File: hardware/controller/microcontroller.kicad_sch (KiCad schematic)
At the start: 41 parts, among them J1 USB_C_Receptacle_USB2.0_14P, J2 IDC-10, SW1 SW_Push, SW2 SW_Push, SW3 SW_Push, U1 SRV05-4, U2 ESP32-C3-WROOM-02, U3 STM32U535RET6, U4 nRF24L01+ 2.4Gz Mini SMD, Y1 8MHz

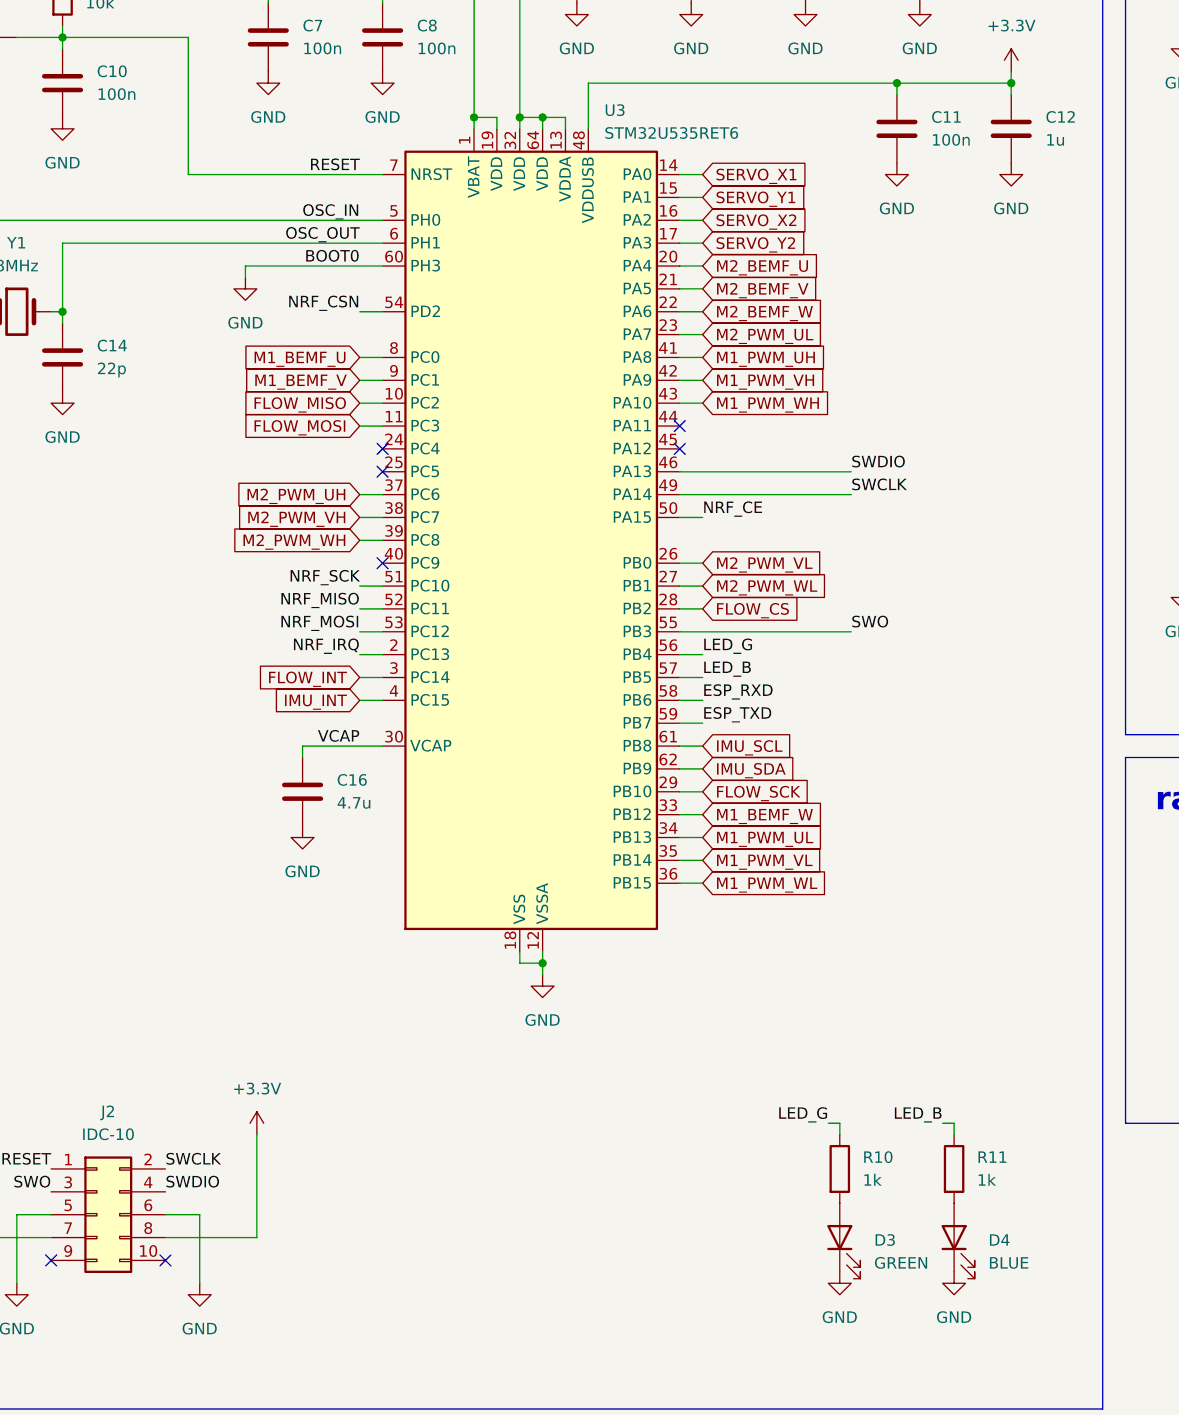
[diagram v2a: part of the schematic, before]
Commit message: change P-MOSFET on the battery enter
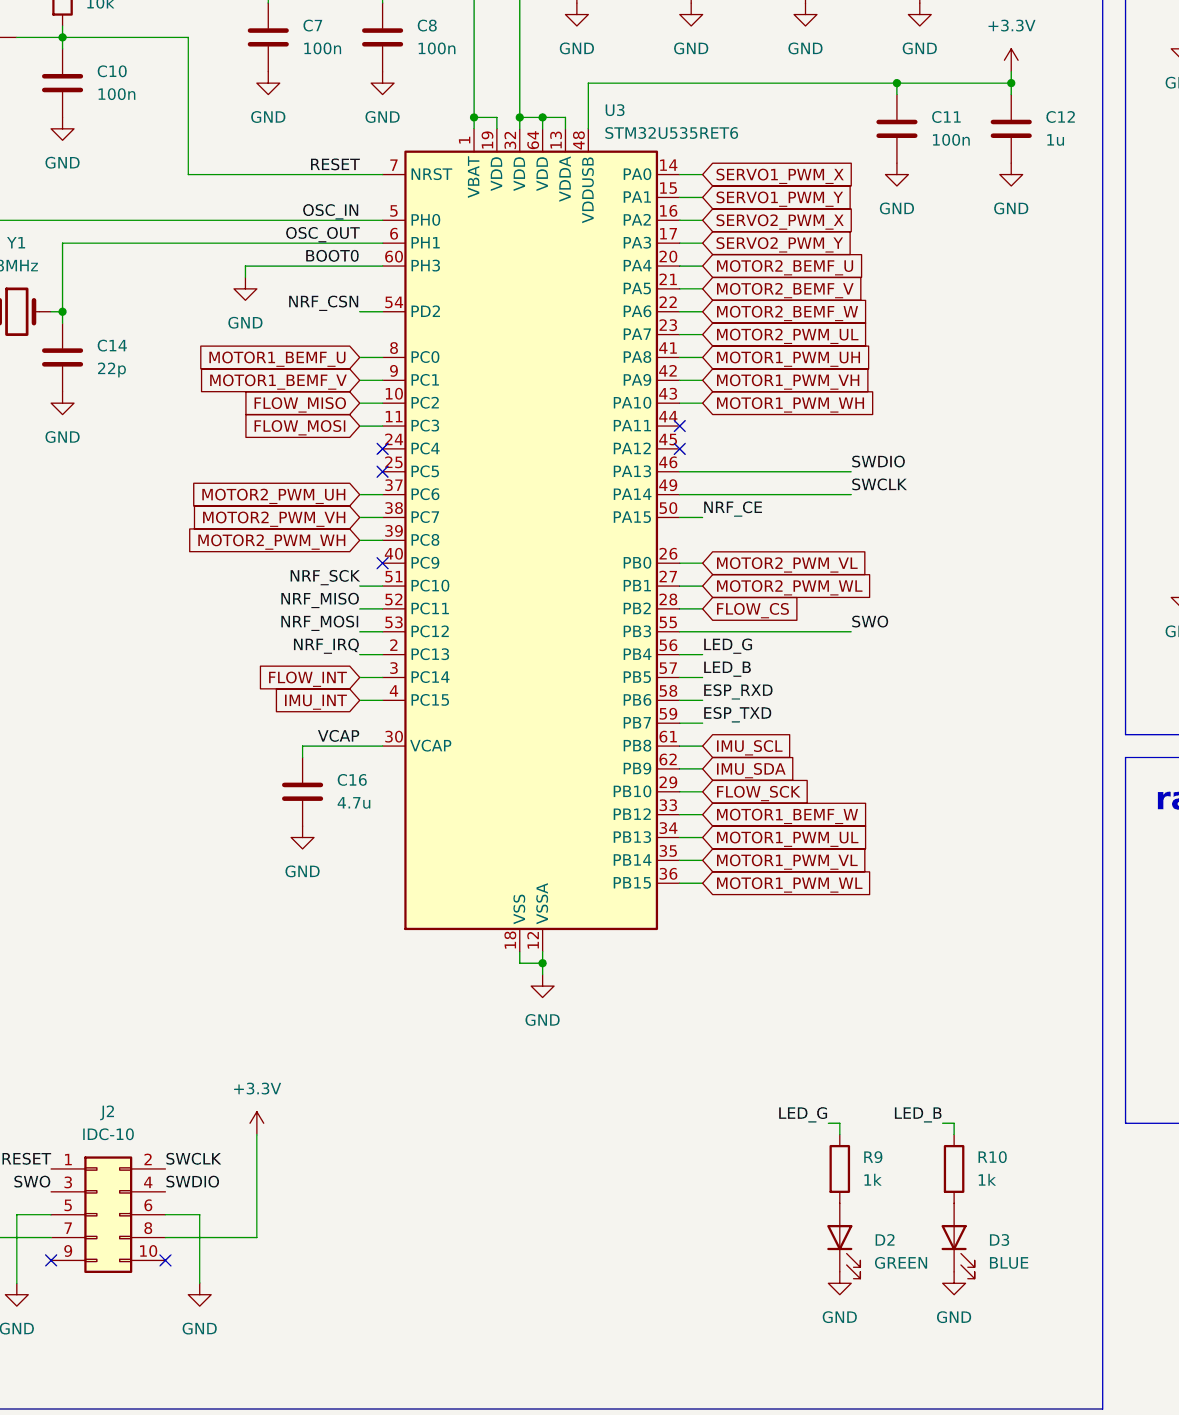
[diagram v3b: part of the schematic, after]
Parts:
- renumbered D3 to D2, D4 to D3, R11 to R10, R10 to R9
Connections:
- net M1_BEMF_U renamed MOTOR1_BEMF_U
- net M1_BEMF_V renamed MOTOR1_BEMF_V
- net M1_BEMF_W renamed MOTOR1_BEMF_W
- net M1_PWM_UH renamed MOTOR1_PWM_UH
- net M1_PWM_UL renamed MOTOR1_PWM_UL
- net M1_PWM_VH renamed MOTOR1_PWM_VH
- net M1_PWM_VL renamed MOTOR1_PWM_VL
- net M1_PWM_WH renamed MOTOR1_PWM_WH
- net M1_PWM_WL renamed MOTOR1_PWM_WL
- net M2_BEMF_U renamed MOTOR2_BEMF_U
- net M2_BEMF_V renamed MOTOR2_BEMF_V
- net M2_BEMF_W renamed MOTOR2_BEMF_W
- net M2_PWM_UH renamed MOTOR2_PWM_UH
- net M2_PWM_UL renamed MOTOR2_PWM_UL
- net M2_PWM_VH renamed MOTOR2_PWM_VH
- net M2_PWM_VL renamed MOTOR2_PWM_VL
- net M2_PWM_WH renamed MOTOR2_PWM_WH
- net M2_PWM_WL renamed MOTOR2_PWM_WL
- net SERVO_X1 renamed SERVO1_PWM_X
- net SERVO_X2 renamed SERVO2_PWM_X
- net SERVO_Y1 renamed SERVO1_PWM_Y
- net SERVO_Y2 renamed SERVO2_PWM_Y
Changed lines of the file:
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@@
 		)
 	)
-	(global_label "M1_PWM_VH"
+	(global_label "MOTOR1_PWM_VH"
 		(shape input)
 		(at 109.22 78.74 0)
@@
 		)
 		(property "Intersheetrefs" "${INTERSHEET_REFS}"
-			(at 123.3932 78.74 0)
+			(at 128.2918 78.74 0)
 			(effects
 				(font
@@
 		)
 	)
-	(global_label "M2_BEMF_U"
+	(global_label "MOTOR2_BEMF_U"
 		(shape input)
 		(at 109.22 66.04 0)
@@
 		)
 		(property "Intersheetrefs" "${INTERSHEET_REFS}"
-			(at 123.0908 66.04 0)
+			(at 127.9894 66.04 0)
 			(effects
 				(font
@@
 		)
 	)
-	(global_label "M1_PWM_VL"
+	(global_label "MOTOR1_PWM_VL"
 		(shape input)
 		(at 109.22 132.08 0)
@@
 		)
 		(property "Intersheetrefs" "${INTERSHEET_REFS}"
-			(at 123.0908 132.08 0)
+			(at 127.9894 132.08 0)
 			(effects
 				(font
@@
 		)
 	)
-	(global_label "M1_BEMF_W"
+	(global_label "MOTOR1_BEMF_W"
 		(shape input)
 		(at 109.22 127 0)
@@
 		)
 		(property "Intersheetrefs" "${INTERSHEET_REFS}"
-			(at 123.2117 127 0)
+			(at 128.1103 127 0)
 			(effects
 				(font
@@
 		)
 	)
-	(global_label "M2_PWM_UH"
+	(global_label "MOTOR2_PWM_UH"
 		(shape input)
 		(at 71.12 91.44 180)
@@
 		)
 		(property "Intersheetrefs" "${INTERSHEET_REFS}"
-			(at 56.7049 91.44 0)
+			(at 51.8063 91.44 0)
 			(effects
 				(font
@@
 		)
 	)
-	(global_label "M2_PWM_WH"
+	(global_label "MOTOR2_PWM_WH"
 		(shape input)
 		(at 71.12 96.52 180)
@@
 		)
 		(property "Intersheetrefs" "${INTERSHEET_REFS}"
-			(at 56.584 96.52 0)
+			(at 51.6854 96.52 0)
 			(effects
 				(font
@@
 		)
 	)
-	(global_label "M2_PWM_VH"
+	(global_label "MOTOR2_PWM_VH"
 		(shape input)
 		(at 71.12 93.98 180)
@@
 		)
 		(property "Intersheetrefs" "${INTERSHEET_REFS}"
-			(at 56.9468 93.98 0)
+			(at 52.0482 93.98 0)
 			(effects
 				(font
@@
 		)
 	)
-	(global_label "M1_PWM_WL"
+	(global_label "MOTOR1_PWM_WL"
 		(shape input)
 		(at 109.22 134.62 0)
@@
 		)
 		(property "Intersheetrefs" "${INTERSHEET_REFS}"
-			(at 123.4536 134.62 0)
+			(at 128.3522 134.62 0)
 			(effects
 				(font
@@
 		)
 	)
-	(global_label "M2_PWM_WL"
+	(global_label "MOTOR2_PWM_WL"
 		(shape input)
 		(at 109.22 101.6 0)
@@
 		)
 		(property "Intersheetrefs" "${INTERSHEET_REFS}"
-			(at 123.4536 101.6 0)
+			(at 128.3522 101.6 0)
 			(effects
 				(font
@@
 		)
 	)
-	(global_label "M2_PWM_UL"
+	(global_label "MOTOR2_PWM_UL"
 		(shape input)
 		(at 109.22 73.66 0)
@@
 		)
 		(property "Intersheetrefs" "${INTERSHEET_REFS}"
-			(at 123.3327 73.66 0)
+			(at 128.2313 73.66 0)
 			(effects
 				(font
@@
 		)
 	)
-	(global_label "M1_PWM_WH"
+	(global_label "MOTOR1_PWM_WH"
 		(shape input)
 		(at 109.22 81.28 0)
@@
 		)
 		(property "Intersheetrefs" "${INTERSHEET_REFS}"
-			(at 123.756 81.28 0)
+			(at 128.6546 81.28 0)
 			(effects
 				(font
@@
 		)
 	)
-	(global_label "SERVO_X2"
+	(global_label "SERVO2_PWM_X"
 		(shape input)
 		(at 109.22 60.96 0)
@@
 		)
 		(property "Intersheetrefs" "${INTERSHEET_REFS}"
-			(at 121.6394 60.96 0)
+			(at 126.7798 60.96 0)
 			(effects
 				(font
@@
 		)
 	)
-	(global_label "M2_BEMF_V"
+	(global_label "MOTOR2_BEMF_V"
 		(shape input)
 		(at 109.22 68.58 0)
@@
 		)
 		(property "Intersheetrefs" "${INTERSHEET_REFS}"
-			(at 122.8489 68.58 0)
+			(at 127.7475 68.58 0)
 			(effects
 				(font
@@
 		)
 	)
-	(global_label "M2_PWM_VL"
+	(global_label "MOTOR2_PWM_VL"
 		(shape input)
 		(at 109.22 99.06 0)
@@
 		)
 		(property "Intersheetrefs" "${INTERSHEET_REFS}"
-			(at 123.0908 99.06 0)
+			(at 127.9894 99.06 0)
 			(effects
 				(font
@@
 		)
 	)
-	(global_label "M2_BEMF_W"
+	(global_label "MOTOR2_BEMF_W"
 		(shape input)
 		(at 109.22 71.12 0)
@@
 		)
 		(property "Intersheetrefs" "${INTERSHEET_REFS}"
-			(at 123.2117 71.12 0)
+			(at 128.1103 71.12 0)
 			(effects
 				(font
@@
 		)
 	)
-	(global_label "M1_BEMF_V"
+	(global_label "MOTOR1_BEMF_V"
 		(shape input)
 		(at 71.12 78.74 180)
@@
 		)
 		(property "Intersheetrefs" "${INTERSHEET_REFS}"
-			(at 57.4911 78.74 0)
+			(at 52.5925 78.74 0)
 			(effects
 				(font
@@
 		)
 	)
-	(global_label "SERVO_Y1"
+	(global_label "SERVO1_PWM_Y"
 		(shape input)
 		(at 109.22 58.42 0)
@@
 		)
 		(property "Intersheetrefs" "${INTERSHEET_REFS}"
-			(at 121.5185 58.42 0)
+			(at 126.6589 58.42 0)
 			(effects
 				(font
@@
 		)
 	)
-	(global_label "SERVO_X1"
+	(global_label "SERVO1_PWM_X"
 		(shape input)
 		(at 109.22 55.88 0)
@@
 		)
 		(property "Intersheetrefs" "${INTERSHEET_REFS}"
-			(at 121.6394 55.88 0)
+			(at 126.7798 55.88 0)
 			(effects
 				(font
@@
 		)
 	)
-	(global_label "SERVO_Y2"
+	(global_label "SERVO2_PWM_Y"
 		(shape input)
 		(at 109.22 63.5 0)
@@
 		)
 		(property "Intersheetrefs" "${INTERSHEET_REFS}"
-			(at 121.5185 63.5 0)
+			(at 126.6589 63.5 0)
 			(effects
 				(font
@@
 		)
 	)
-	(global_label "M1_PWM_UH"
+	(global_label "MOTOR1_PWM_UH"
 		(shape input)
 		(at 109.22 76.2 0)
@@
 		)
 		(property "Intersheetrefs" "${INTERSHEET_REFS}"
-			(at 123.6351 76.2 0)
+			(at 128.5337 76.2 0)
 			(effects
 				(font
@@
 		)
 	)
-	(global_label "M1_BEMF_U"
+	(global_label "MOTOR1_BEMF_U"
 		(shape input)
 		(at 71.12 76.2 180)
@@
 		)
 		(property "Intersheetrefs" "${INTERSHEET_REFS}"
-			(at 57.2492 76.2 0)
+			(at 52.3506 76.2 0)
 			(effects
 				(font
@@
 		)
 	)
-	(global_label "M1_PWM_UL"
+	(global_label "MOTOR1_PWM_UL"
 		(shape input)
 		(at 109.22 129.54 0)
@@
 		)
 		(property "Intersheetrefs" "${INTERSHEET_REFS}"
-			(at 123.3327 129.54 0)
+			(at 128.2313 129.54 0)
 			(effects
 				(font
@@
 		(dnp no)
 		(fields_autoplaced yes)
-		(property "Reference" "#PWR044"
+		(property "Reference" "#PWR043"
 			(at 124.46 184.15 0)
 			(effects
@@
 			(project "controller"
 				(path "/b81e4285-7ba7-4843-ab37-49bb8c6c135f/e4f7bb70-a8bb-48a9-92b7-fd3dfb9899ca"
-					(reference "#PWR044")
+					(reference "#PWR043")
 					(unit 1)
 				)
@@
 		(dnp no)
 		(fields_autoplaced yes)
-		(property "Reference" "D3"
+		(property "Reference" "D2"
 			(at 128.27 174.3074 90)
 			(effects
@@
 			(project "controller"
 				(path "/b81e4285-7ba7-4843-ab37-49bb8c6c135f/e4f7bb70-a8bb-48a9-92b7-fd3dfb9899ca"
-					(reference "D3")
+					(reference "D2")
 					(unit 1)
 				)
@@
 		(dnp no)
 		(fields_autoplaced yes)
-		(property "Reference" "#PWR045"
+		(property "Reference" "#PWR044"
 			(at 137.16 184.15 0)
 			(effects
@@
 			(project "controller"
 				(path "/b81e4285-7ba7-4843-ab37-49bb8c6c135f/e4f7bb70-a8bb-48a9-92b7-fd3dfb9899ca"
-					(reference "#PWR045")
+					(reference "#PWR044")
 					(unit 1)
 				)
@@
 		(dnp no)
 		(fields_autoplaced yes)
-		(property "Reference" "#PWR047"
+		(property "Reference" "#PWR046"
 			(at 53.34 185.42 0)
 			(effects
@@
 			(project "controller"
 				(path "/b81e4285-7ba7-4843-ab37-49bb8c6c135f/e4f7bb70-a8bb-48a9-92b7-fd3dfb9899ca"
-					(reference "#PWR047")
+					(reference "#PWR046")
 					(unit 1)
 				)
@@
 		(dnp no)
 		(fields_autoplaced yes)
-		(property "Reference" "R11"
+		(property "Reference" "R10"
 			(at 139.7 165.0999 0)
 			(effects
@@
 			(project "controller"
 				(path "/b81e4285-7ba7-4843-ab37-49bb8c6c135f/e4f7bb70-a8bb-48a9-92b7-fd3dfb9899ca"
-					(reference "R11")
+					(reference "R10")
 					(unit 1)
 				)
@@
 		(dnp no)
 		(fields_autoplaced yes)
-		(property "Reference" "D4"
+		(property "Reference" "D3"
 			(at 140.97 174.3074 90)
 			(effects
@@
 			(project "controller"
 				(path "/b81e4285-7ba7-4843-ab37-49bb8c6c135f/e4f7bb70-a8bb-48a9-92b7-fd3dfb9899ca"
-					(reference "D4")
+					(reference "D3")
 					(unit 1)
 				)
@@
 		(dnp no)
 		(fields_autoplaced yes)
-		(property "Reference" "R10"
+		(property "Reference" "R9"
 			(at 127 165.0999 0)
 			(effects
@@
 			(project "controller"
 				(path "/b81e4285-7ba7-4843-ab37-49bb8c6c135f/e4f7bb70-a8bb-48a9-92b7-fd3dfb9899ca"
-					(reference "R10")
+					(reference "R9")
 					(unit 1)
 				)
@@
 		(dnp no)
 		(fields_autoplaced yes)
-		(property "Reference" "#PWR046"
+		(property "Reference" "#PWR045"
 			(at 33.02 185.42 0)
 			(effects
@@
 			(project "controller"
 				(path "/b81e4285-7ba7-4843-ab37-49bb8c6c135f/e4f7bb70-a8bb-48a9-92b7-fd3dfb9899ca"
-					(reference "#PWR046")
+					(reference "#PWR045")
 					(unit 1)
 				)

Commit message: footprints, layout
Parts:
- J1: footprint (none) -> Connector_USB:USB_C_Receptacle_GCT_USB4085
- J2: footprint (none) -> Connector_IDC:IDC-Header_2x05_P2.54mm_Horizontal
- R5, R6: footprint (none) -> Resistor_SMD:R_0603_1608Metric
- SW1, SW2, SW3: footprint (none) -> Button_Switch_THT:SW_Tactile_SPST_Angled_PTS645Vx58-2LFS
- Y1: footprint goose:oscillator_5032_2 -> Crystal:Crystal_SMD_5032-2Pin_5.0x3.2mm
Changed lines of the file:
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@@
 	(title_block
 		(title "Hogger2 Controller")
-		(date "2024-11-01")
+		(date "2024-11-03")
 		(rev "V1.0")
 		(comment 4 "Author: Eryk Możdżeń")
@@
 			)
 		)
-		(property "Footprint" ""
+		(property "Footprint" "Connector_IDC:IDC-Header_2x05_P2.54mm_Horizontal"
 			(at 41.91 171.45 0)
 			(effects
@@
 			)
 		)
-		(property "Footprint" ""
+		(property "Footprint" "Resistor_SMD:R_0603_1608Metric"
 			(at 233.68 77.978 90)
 			(effects
@@
 			)
 		)
-		(property "Footprint" ""
+		(property "Footprint" "Button_Switch_THT:SW_Tactile_SPST_Angled_PTS645Vx58-2LFS"
 			(at 27.94 35.56 0)
 			(effects
@@
 			)
 		)
-		(property "Footprint" ""
+		(property "Footprint" "Button_Switch_THT:SW_Tactile_SPST_Angled_PTS645Vx58-2LFS"
 			(at 168.91 95.25 0)
 			(effects
@@
 			)
 		)
-		(property "Footprint" ""
+		(property "Footprint" "Connector_USB:USB_C_Receptacle_GCT_USB4085"
 			(at 260.35 86.36 0)
 			(effects
@@
 			)
 		)
-		(property "Footprint" ""
+		(property "Footprint" "Resistor_SMD:R_0603_1608Metric"
 			(at 233.68 76.962 90)
 			(effects
@@
 			)
 		)
-		(property "Footprint" ""
+		(property "Footprint" "Button_Switch_THT:SW_Tactile_SPST_Angled_PTS645Vx58-2LFS"
 			(at 168.91 34.29 0)
 			(effects
@@
 			)
 		)
-		(property "Footprint" "goose:oscillator_5032_2"
+		(property "Footprint" "Crystal:Crystal_SMD_5032-2Pin_5.0x3.2mm"
 			(at 33.02 71.12 0)
 			(effects
